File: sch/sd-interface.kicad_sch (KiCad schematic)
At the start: 31 parts, among them J15 F32Q-1A7H1-11022, J16 MEM2075-00-140-01-A, J17 691137710002, Q1 Q_PMOS_GSD, U10 CD4043BDR, U11 TPS22919DCKR, U8 MAX4996LETG_

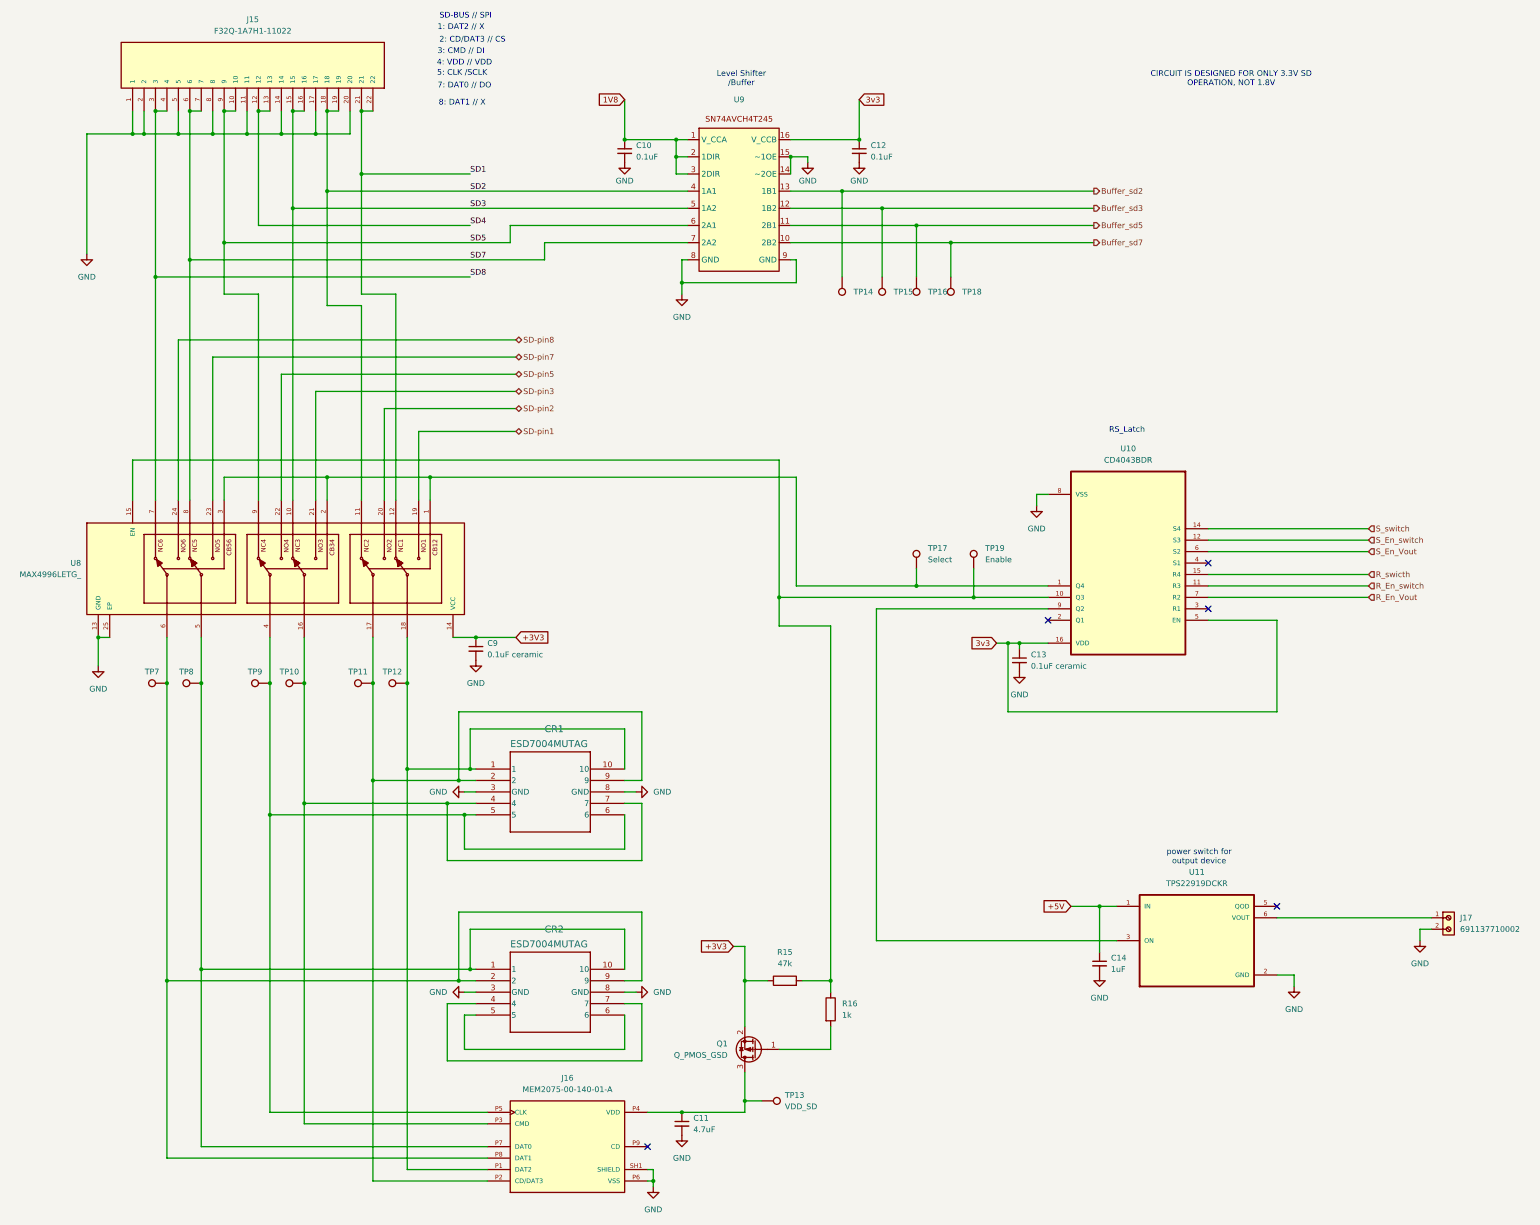
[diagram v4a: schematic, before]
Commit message: added more footprints and added to pcb
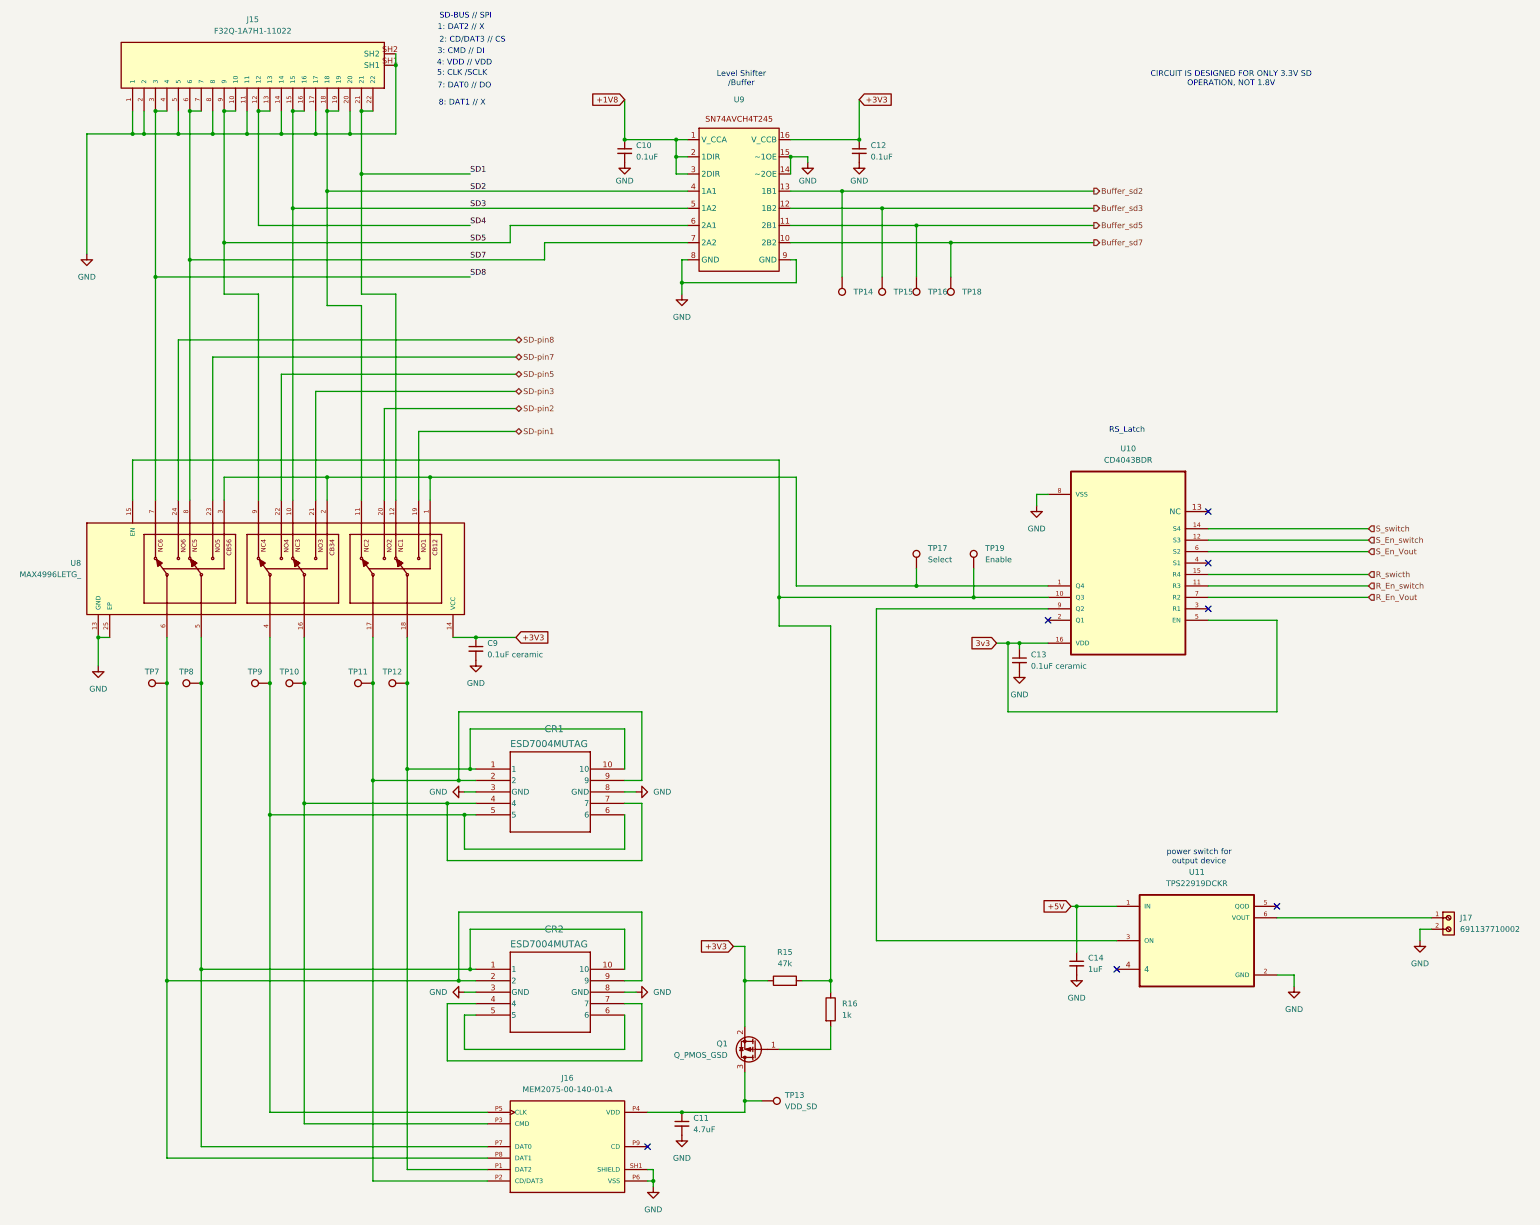
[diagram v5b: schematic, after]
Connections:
- net +3V3: now also C12.1, U9.16 (V_CCB)
- net 3v3: no longer C12.1, U9.16 (V_CCB)
- net GND: now also J15.SH1, J15.SH2
- net 1V8 renamed +1V8
- no-connect marks 5 -> 7
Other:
- moved on the sheet: C14
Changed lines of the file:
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@@
 	)
 	(junction
-		(at 275.59 213.36)
-		(diameter 0)
-		(color 0 0 0 0)
-	)
-	(junction
 		(at 135.89 227.33)
 		(diameter 0)
@@
 	)
 	(junction
+		(at 119.38 26.67)
+		(diameter 0)
+		(color 0 0 0 0)
+	)
+	(junction
 		(at 63.5 41.91)
 		(diameter 0)
@@
 	)
 	(junction
+		(at 270.51 213.36)
+		(diameter 0)
+		(color 0 0 0 0)
+	)
+	(junction
 		(at 222.25 43.18)
 		(diameter 0)
@@
 	)
 	(junction
+		(at 109.22 41.91)
+		(diameter 0)
+		(color 0 0 0 0)
+	)
+	(junction
 		(at 182.88 259.08)
 		(diameter 0)
@@
 	)
 	(no_connect
+		(at 299.72 125.73)
+	)
+	(no_connect
 		(at 314.96 213.36)
 	)
@@
 	)
 	(no_connect
+		(at 279.4 227.33)
+	)
+	(no_connect
 		(at 175.26 266.7)
 	)
@@
 	(wire
 		(pts
-			(xy 279.4 213.36) (xy 275.59 213.36)
-		)
-		(stroke
-			(width 0)
-			(type default)
-		)
-	)
-	(wire
-		(pts
 			(xy 119.38 77.47) (xy 111.76 77.47)
 		)
@@
 	(wire
 		(pts
-			(xy 275.59 223.52) (xy 275.59 213.36)
+			(xy 270.51 223.52) (xy 270.51 213.36)
 		)
 		(stroke
@@
 	(wire
 		(pts
-			(xy 269.24 213.36) (xy 275.59 213.36)
+			(xy 269.24 213.36) (xy 270.51 213.36)
 		)
 		(stroke
@@
 	(wire
 		(pts
+			(xy 109.22 41.91) (xy 119.38 41.91)
+		)
+		(stroke
+			(width 0)
+			(type default)
+		)
+	)
+	(wire
+		(pts
 			(xy 207.01 58.42) (xy 227.33 58.42)
 		)
@@
 	(wire
 		(pts
+			(xy 270.51 213.36) (xy 279.4 213.36)
+		)
+		(stroke
+			(width 0)
+			(type default)
+		)
+	)
+	(wire
+		(pts
 			(xy 71.12 41.91) (xy 78.74 41.91)
 		)
@@
 	(wire
 		(pts
+			(xy 119.38 41.91) (xy 119.38 26.67)
+		)
+		(stroke
+			(width 0)
+			(type default)
+		)
+	)
+	(wire
+		(pts
 			(xy 133.35 229.87) (xy 137.16 229.87)
 		)
@@
 	(wire
 		(pts
+			(xy 119.38 26.67) (xy 119.38 24.13)
+		)
+		(stroke
+			(width 0)
+			(type default)
+		)
+	)
+	(wire
+		(pts
 			(xy 184.15 66.04) (xy 152.4 66.04)
 		)
@@
 		)
 	)
-	(global_label "3v3"
+	(global_label "+3V3"
 		(shape input)
 		(at 222.25 34.29 0)
@@
 		)
 		(property "Intersheetrefs" "${INTERSHEET_REFS}"
-			(at 228.6218 34.29 0)
+			(at 230.3152 34.29 0)
 			(effects
 				(font
@@
 		)
 	)
-	(global_label "1V8"
+	(global_label "+1V8"
 		(shape input)
 		(at 170.18 34.29 180)
@@
 		)
 		(property "Intersheetrefs" "${INTERSHEET_REFS}"
-			(at 163.6872 34.29 0)
+			(at 162.1148 34.29 0)
 			(effects
 				(font
@@
 	(symbol
 		(lib_id "Device:C_Small")
-		(at 275.59 226.06 0)
+		(at 270.51 226.06 0)
 		(unit 1)
 		(exclude_from_sim no)
@@
 		(fields_autoplaced yes)
 		(property "Reference" "C14"
-			(at 278.13 224.7962 0)
+			(at 273.05 224.7962 0)
 			(effects
 				(font
@@
 		)
 		(property "Value" "1uF"
-			(at 278.13 227.3362 0)
+			(at 273.05 227.3362 0)
 			(effects
 				(font
@@
 		)
 		(property "Footprint" "Capacitor_SMD:C_0603_1608Metric"
-			(at 275.59 226.06 0)
+			(at 270.51 226.06 0)
 			(effects
 				(font
@@
 		)
 		(property "Datasheet" "~"
-			(at 275.59 226.06 0)
+			(at 270.51 226.06 0)
 			(effects
 				(font
@@
 		)
 		(property "Description" "Unpolarized capacitor, small symbol"
-			(at 275.59 226.06 0)
+			(at 270.51 226.06 0)
 			(effects
 				(font
@@
 		)
 		(property "MPN" "CL10B105KP8NNNC"
-			(at 275.59 226.06 0)
+			(at 270.51 226.06 0)
 			(effects
 				(font
@@
 		(pin "1"
 		)
+		(pin "4"
+		)
 		(instances
 			(project "audiograb"
@@
 		(pin "22"
 		)
+		(pin "SH1"
+		)
+		(pin "SH2"
+		)
 		(instances
 			(project "audiograb"
@@
 	(symbol
 		(lib_id "power:GND")
-		(at 275.59 228.6 0)
+		(at 270.51 228.6 0)
 		(unit 1)
 		(exclude_from_sim no)
@@
 		(fields_autoplaced yes)
 		(property "Reference" "#PWR055"
-			(at 275.59 234.95 0)
+			(at 270.51 234.95 0)
 			(effects
 				(font
@@
 		)
 		(property "Value" "GND"
-			(at 275.59 233.68 0)
+			(at 270.51 233.68 0)
 			(effects
 				(font
@@
 		)
 		(property "Footprint" ""
-			(at 275.59 228.6 0)
+			(at 270.51 228.6 0)
 			(effects
 				(font
@@
 		)
 		(property "Datasheet" ""
-			(at 275.59 228.6 0)
+			(at 270.51 228.6 0)
 			(effects
 				(font
@@
 		)
 		(property "Description" "Power symbol creates a global label with name \"GND\" , ground"
-			(at 275.59 228.6 0)
+			(at 270.51 228.6 0)
 			(effects
 				(font
@@
 		(pin "2"
 		)
+		(pin "13"
+		)
 		(instances

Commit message: added ports to powersupply
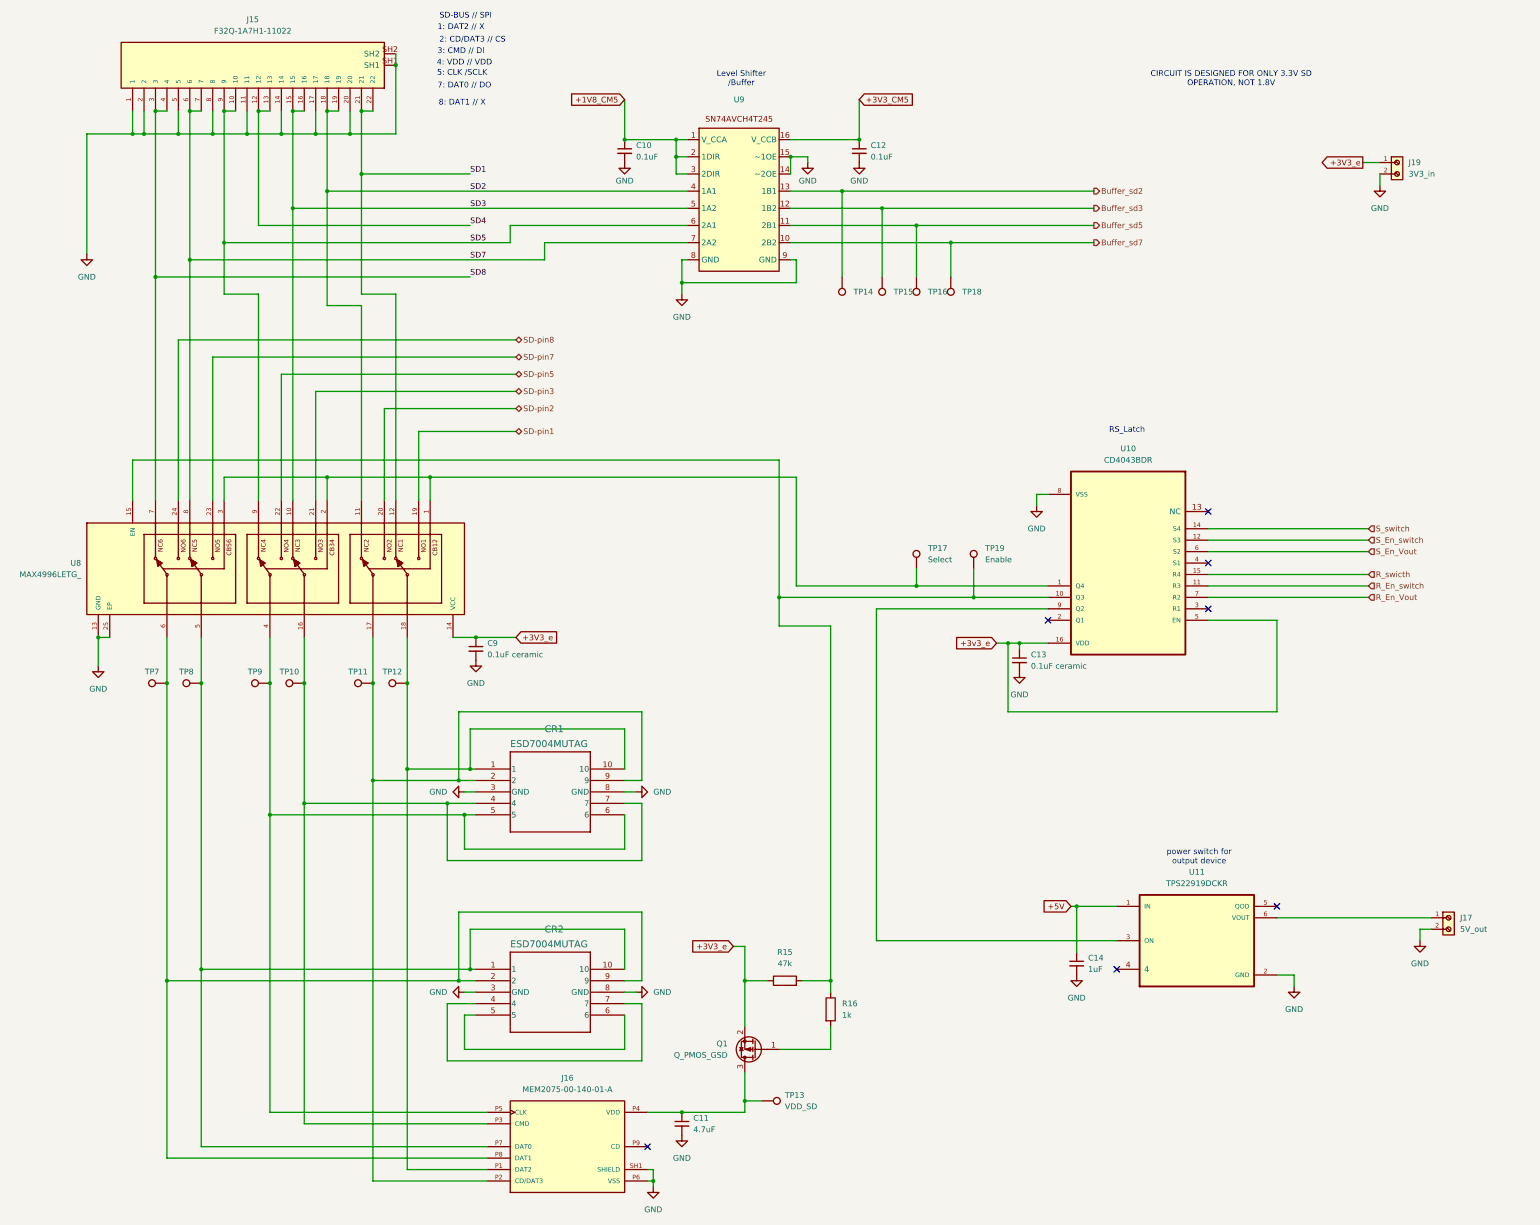
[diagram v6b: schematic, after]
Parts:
- added J19: 3V3_in, 691137710002:691137710002, symbol 691137710002:691137710002
- J17: value 691137710002 -> 5V_out
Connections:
- net GND: now also J19.2
- net +1V8 renamed +1V8_CM5
- net +3V3 renamed +3V3_e
- net +3V3_e: now also J19.1; no longer C12.1, U9.16 (V_CCB)
- net 3v3 renamed +3v3_e
- new net +3V3_CM5: C12.1, U9.16 (V_CCB)

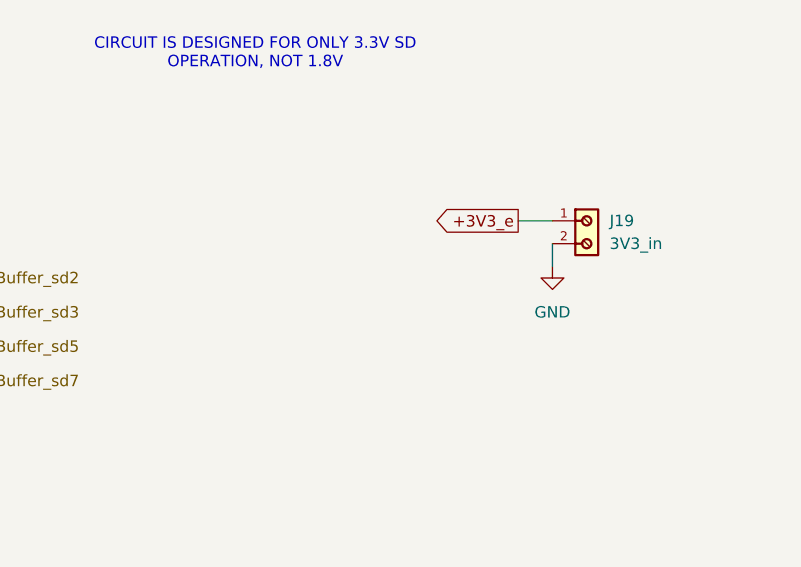
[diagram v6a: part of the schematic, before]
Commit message: added capacitor on 3.3V in
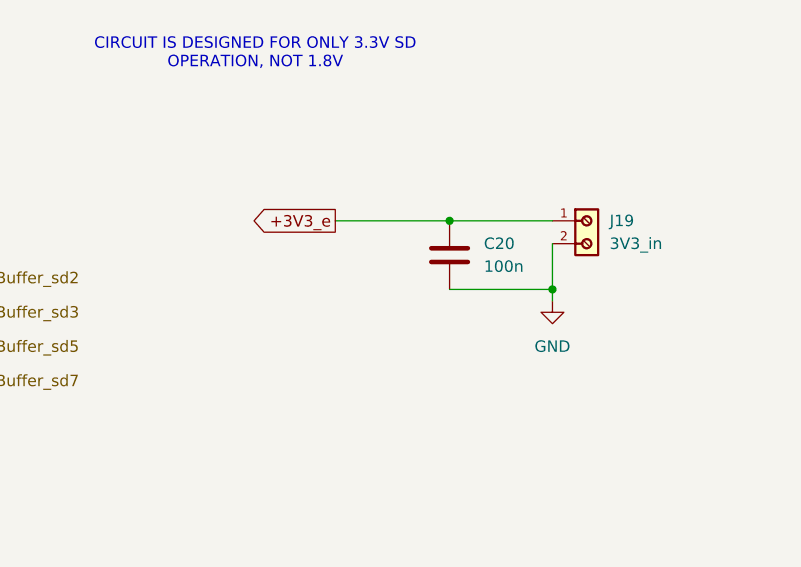
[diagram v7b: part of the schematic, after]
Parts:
- added C20: 100n, Capacitor_SMD:C_0603_1608Metric, symbol Device:C
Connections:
- net +3V3_e: now also C20.1
- net GND: now also C20.2
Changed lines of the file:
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@@
 	)
 	(junction
+		(at 326.39 48.26)
+		(diameter 0)
+		(color 0 0 0 0)
+	)
+	(junction
 		(at 114.3 185.42)
 		(diameter 0)
@@
 	)
 	(junction
+		(at 337.82 55.88)
+		(diameter 0)
+		(color 0 0 0 0)
+	)
+	(junction
 		(at 91.44 163.83)
 		(diameter 0)
@@
 	(wire
 		(pts
-			(xy 334.01 48.26) (xy 337.82 48.26)
+			(xy 313.69 48.26) (xy 326.39 48.26)
 		)
 		(stroke
@@
 	(wire
 		(pts
-			(xy 337.82 50.8) (xy 337.82 53.34)
+			(xy 337.82 50.8) (xy 337.82 55.88)
 		)
 		(stroke
@@
 	(wire
 		(pts
+			(xy 326.39 55.88) (xy 337.82 55.88)
+		)
+		(stroke
+			(width 0)
+			(type default)
+		)
+	)
+	(wire
+		(pts
 			(xy 299.72 144.78) (xy 335.28 144.78)
 		)
@@
 	(wire
 		(pts
+			(xy 326.39 48.26) (xy 337.82 48.26)
+		)
+		(stroke
+			(width 0)
+			(type default)
+		)
+	)
+	(wire
+		(pts
 			(xy 299.72 139.7) (xy 335.28 139.7)
 		)
@@
 	(wire
 		(pts
+			(xy 337.82 55.88) (xy 337.82 57.15)
+		)
+		(stroke
+			(width 0)
+			(type default)
+		)
+	)
+	(wire
+		(pts
 			(xy 99.06 190.5) (xy 130.81 190.5)
 		)
@@
 	(global_label "+3V3_e"
 		(shape output)
-		(at 334.01 48.26 180)
+		(at 313.69 48.26 180)
 		(fields_autoplaced yes)
 		(effects
@@
 		)
 		(property "Intersheetrefs" "${INTERSHEET_REFS}"
-			(at 323.8886 48.26 0)
+			(at 303.5686 48.26 0)
 			(effects
 				(font
@@
 	(symbol
 		(lib_id "power:GND")
-		(at 337.82 53.34 0)
+		(at 337.82 57.15 0)
 		(unit 1)
 		(exclude_from_sim no)
@@
 		(fields_autoplaced yes)
 		(property "Reference" "#PWR07"
-			(at 337.82 59.69 0)
+			(at 337.82 63.5 0)
 			(effects
 				(font
@@
 		)
 		(property "Value" "GND"
-			(at 337.82 58.42 0)
+			(at 337.82 62.23 0)
 			(effects
 				(font
@@
 		)
 		(property "Footprint" ""
-			(at 337.82 53.34 0)
+			(at 337.82 57.15 0)
 			(effects
 				(font
@@
 		)
 		(property "Datasheet" ""
-			(at 337.82 53.34 0)
+			(at 337.82 57.15 0)
 			(effects
 				(font
@@
 		)
 		(property "Description" "Power symbol creates a global label with name \"GND\" , ground"
-			(at 337.82 53.34 0)
+			(at 337.82 57.15 0)
 			(effects
 				(font
@@
 					(unit 1)
 				)
+			)
+		)
+	)
+	(symbol
+		(lib_id "Device:C")
+		(at 326.39 52.07 0)
+		(unit 1)
+		(exclude_from_sim no)
+		(in_bom yes)
+		(on_board yes)
+		(dnp no)
+		(property "Reference" "C20"
+			(at 330.2 50.7999 0)
+			(effects
+				(font
+					(size 1.27 1.27)
+				)
+				(justify left)
+			)
+		)
+		(property "Value" "100n"
+			(at 330.2 53.3399 0)
+			(effects
+				(font
+					(size 1.27 1.27)
+				)
+				(justify left)
+			)
+		)
+		(property "Footprint" "Capacitor_SMD:C_0603_1608Metric"
+			(at 327.3552 55.88 0)
+			(effects
+				(font
+					(size 1.27 1.27)
+				)
+				(hide yes)
+			)
+		)
+		(property "Datasheet" "~"
+			(at 326.39 52.07 0)
+			(effects
+				(font
+					(size 1.27 1.27)
+				)
+				(hide yes)
+			)
+		)
+		(property "Description" "Unpolarized capacitor"
+			(at 326.39 52.07 0)
+			(effects
+				(font
+					(size 1.27 1.27)
+				)
+				(hide yes)
+			)
+		)
+		(property "MPN" "C0603C104K3RACTU"
+			(at 326.39 52.07 0)
+			(effects
+				(font
+					(size 1.27 1.27)
+				)
+				(hide yes)
+			)
+		)
+		(pin "2"
+		)
+		(pin "1"
+		)
+		(instances
+			(project "audiograb"
+				(path "/c46c2311-6d4b-411d-b012-c7730eac136d/6c55ccce-577d-49c2-8294-3a5d8e11981e"
+					(reference "C20")
+					(unit 1)
+				)
